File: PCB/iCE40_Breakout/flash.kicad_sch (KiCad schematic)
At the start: 43 parts, among them J1 prog_hdr, Q10 L2N7002SLLT1G, Q11 L2N7002SLLT1G, Q12 L2N7002SLLT1G, Q13 L2N7002SLLT1G, Q14 L2N7002SLLT1G, Q15 L2N7002SLLT1G, Q16 L2N7002SLLT1G, Q6 L2N7002SLLT1G, Q7 L2N7002SLLT1G, Q8 L2N7002SLLT1G, Q9 L2N7002SLLT1G, U6 W25Q128JVS

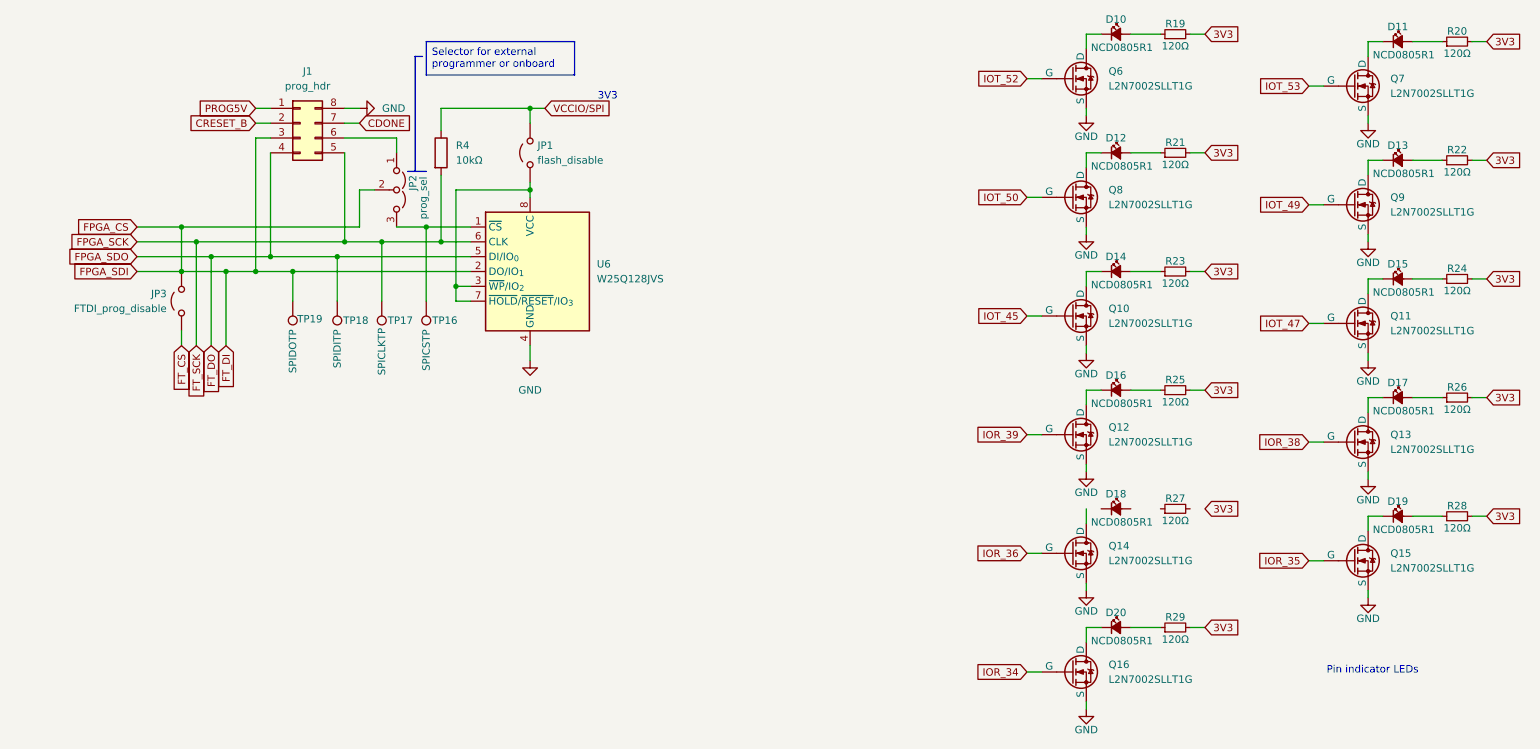
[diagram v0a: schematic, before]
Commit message: Added sheet information, and fixed ERC errors
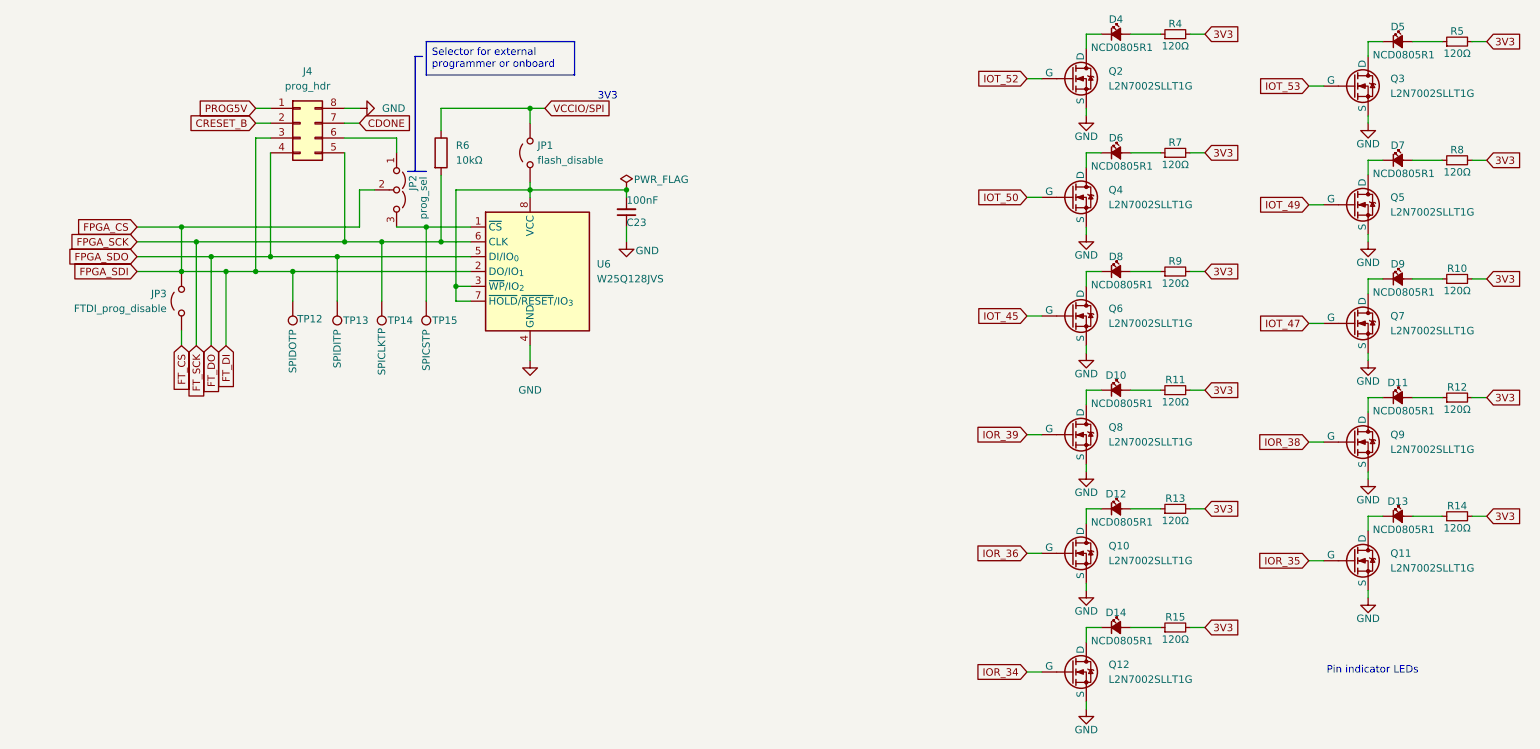
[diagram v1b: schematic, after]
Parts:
- added C23: 100nF, Capacitor_SMD:C_0402_1005Metric, symbol Device:C_Small
- renumbered D16 to D10, D17 to D11, D18 to D12, D19 to D13, D20 to D14, D10 to D4, D11 to D5, D12 to D6, D13 to D7, D14 to D8, D15 to D9, J1 to J4, Q14 to Q10, Q15 to Q11, Q16 to Q12, Q6 to Q2, Q7 to Q3, Q8 to Q4, Q9 to Q5, Q10 to Q6, Q11 to Q7, Q12 to Q8, Q13 to Q9, R24 to R10, R25 to R11, R26 to R12, R27 to R13, R28 to R14, R29 to R15, R19 to R4, R20 to R5, R4 to R6, R21 to R7, R22 to R8, R23 to R9, TP19 to TP12, TP18 to TP13, TP17 to TP14, TP16 to TP15
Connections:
- net 3V3: now also R13.2
- net GND: now also C23.1
- net at R13.1: now also D12.2 (A)
- net at JP1.1 (A), U6.3 (~{WP}/IO_{2}), U6.7 (~{HOLD}/~{RESET}/IO_{3})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: now also C23.2
- net at D12.1 (K): now also Q10.1 (D)
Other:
- company: (none) -> S3I
- title: (none) -> iCE40 Breakout

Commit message: Added missing footprints
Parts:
- J4: footprint (none) -> Connector_PinHeader_2.54mm:PinHeader_2x04_P2.54mm_Vertical
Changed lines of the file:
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@@
 			)
 		)
-		(property "Footprint" ""
+		(property "Footprint" "Connector_PinHeader_2.54mm:PinHeader_2x04_P2.54mm_Vertical"
 			(at 69.85 34.29 0)
 			(effects

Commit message: Changed LED footprints to be from LED lib, and not the Diode lib
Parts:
- D10, D11, D12, D13, D14, D4, D5, D6, D7, D8, D9: footprint Diode_SMD:D_0805_2012Metric -> LED_SMD:LED_0805_2012Metric
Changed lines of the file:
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@@
 			)
 		)
-		(property "Footprint" "Diode_SMD:D_0805_2012Metric"
+		(property "Footprint" "LED_SMD:LED_0805_2012Metric"
 			(at 209.55 120.65 90)
 			(effects
@@
 			)
 		)
-		(property "Footprint" "Diode_SMD:D_0805_2012Metric"
+		(property "Footprint" "LED_SMD:LED_0805_2012Metric"
 			(at 209.55 19.05 90)
 			(effects
@@
 			)
 		)
-		(property "Footprint" "Diode_SMD:D_0805_2012Metric"
+		(property "Footprint" "LED_SMD:LED_0805_2012Metric"
 			(at 209.55 39.37 90)
 			(effects
@@
 			)
 		)
-		(property "Footprint" "Diode_SMD:D_0805_2012Metric"
+		(property "Footprint" "LED_SMD:LED_0805_2012Metric"
 			(at 257.81 81.28 90)
 			(effects
@@
 			)
 		)
-		(property "Footprint" "Diode_SMD:D_0805_2012Metric"
+		(property "Footprint" "LED_SMD:LED_0805_2012Metric"
 			(at 257.81 60.96 90)
 			(effects
@@
 			)
 		)
-		(property "Footprint" "Diode_SMD:D_0805_2012Metric"
+		(property "Footprint" "LED_SMD:LED_0805_2012Metric"
 			(at 209.55 59.69 90)
 			(effects
@@
 			)
 		)
-		(property "Footprint" "Diode_SMD:D_0805_2012Metric"
+		(property "Footprint" "LED_SMD:LED_0805_2012Metric"
 			(at 257.81 101.6 90)
 			(effects
@@
 			)
 		)
-		(property "Footprint" "Diode_SMD:D_0805_2012Metric"
+		(property "Footprint" "LED_SMD:LED_0805_2012Metric"
 			(at 209.55 100.33 90)
 			(effects
@@
 			)
 		)
-		(property "Footprint" "Diode_SMD:D_0805_2012Metric"
+		(property "Footprint" "LED_SMD:LED_0805_2012Metric"
 			(at 209.55 80.01 90)
 			(effects
@@
 			)
 		)
-		(property "Footprint" "Diode_SMD:D_0805_2012Metric"
+		(property "Footprint" "LED_SMD:LED_0805_2012Metric"
 			(at 257.81 40.64 90)
 			(effects
@@
 			)
 		)
-		(property "Footprint" "Diode_SMD:D_0805_2012Metric"
+		(property "Footprint" "LED_SMD:LED_0805_2012Metric"
 			(at 257.81 20.32 90)
 			(effects

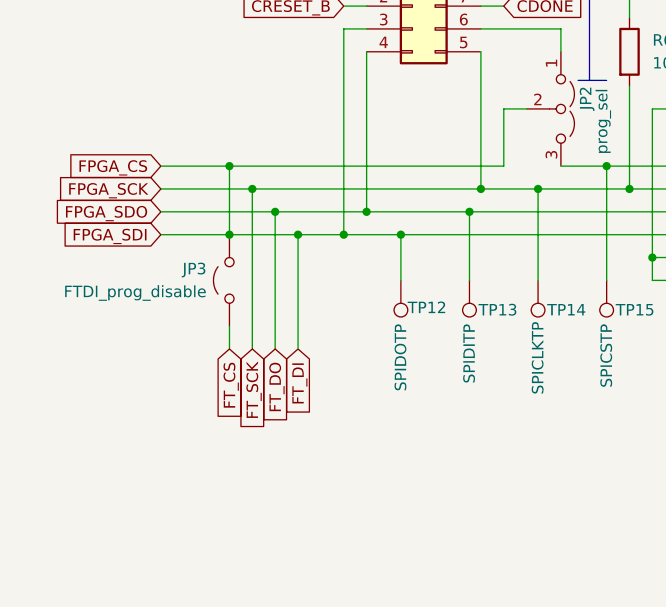
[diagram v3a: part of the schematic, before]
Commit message: Cleaned up SPI flash lines, and removed error where CS was shorted to DI
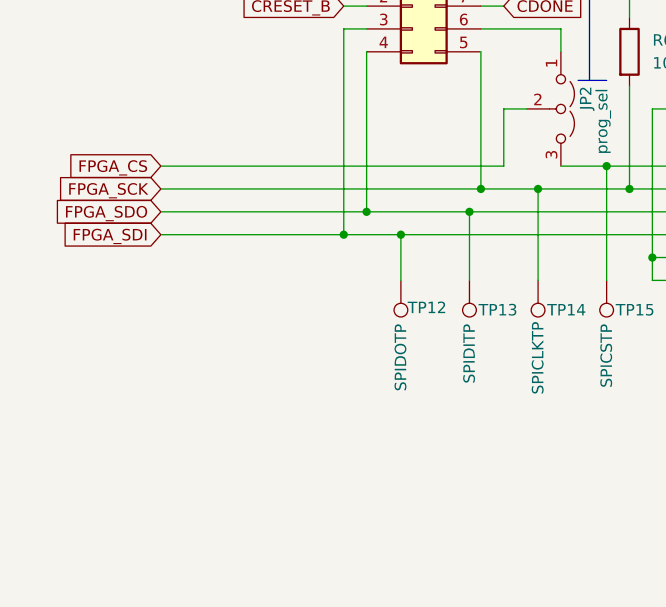
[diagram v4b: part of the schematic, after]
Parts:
- removed JP3: FTDI_prog_disable, Connector_PinSocket_2.54mm:PinSocket_1x02_P2.54mm_Vertical, symbol Jumper:Jumper_2_Open
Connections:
- net FPGA_CS: no longer J4.3 (Pin_3), TP12.1, U6.2 (DO/IO_{1})
- new net FPGA_SDI: J4.3 (Pin_3), TP12.1, U6.2 (DO/IO_{1})

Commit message: Changed jumper footprint to come from jumper library, not generic connector
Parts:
- added R30: 10kΩ, Resistor_SMD:R_0603_1608Metric, symbol Device:R_Small
- JP1: footprint Connector_PinSocket_2.54mm:PinSocket_1x02_P2.54mm_Vertical -> TestPoint:TestPoint_2Pads_Pitch2.54mm_Drill0.8mm
- R6: symbol Device:R -> Device:R_Small
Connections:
- net at C23.2, JP1.1 (A), U6.8 (VCC): now also R30.2; no longer U6.3 (~{WP}/IO_{2}), U6.7 (~{HOLD}/~{RESET}/IO_{3})
- new net: R30.1, U6.3 (~{WP}/IO_{2}), U6.7 (~{HOLD}/~{RESET}/IO_{3})
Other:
- moved on the sheet: R6
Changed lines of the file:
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@@
 	(wire
 		(pts
-			(xy 93.98 43.18) (xy 93.98 54.61)
+			(xy 93.98 39.37) (xy 93.98 54.61)
 		)
 		(stroke
@@
 	(wire
 		(pts
+			(xy 105.41 45.72) (xy 109.22 45.72)
+		)
+		(stroke
+			(width 0)
+			(type default)
+		)
+	)
+	(wire
+		(pts
 			(xy 96.52 62.23) (xy 96.52 64.77)
 		)
@@
 	(wire
 		(pts
-			(xy 96.52 45.72) (xy 109.22 45.72)
+			(xy 96.52 45.72) (xy 100.33 45.72)
 		)
 		(stroke
@@
 	(wire
 		(pts
-			(xy 93.98 31.75) (xy 93.98 35.56)
+			(xy 93.98 31.75) (xy 93.98 34.29)
 		)
 		(stroke
@@
 	)
 	(symbol
-		(lib_id "Device:R")
-		(at 93.98 39.37 0)
+		(lib_id "Device:R_Small")
+		(at 93.98 36.83 0)
 		(unit 1)
 		(exclude_from_sim no)
@@
 		(fields_autoplaced yes)
 		(property "Reference" "R6"
-			(at 96.52 38.0999 0)
+			(at 96.52 35.5599 0)
 			(effects
 				(font
@@
 		)
 		(property "Value" "10kΩ"
-			(at 96.52 40.6399 0)
+			(at 96.52 38.0999 0)
 			(effects
 				(font
@@
 		)
 		(property "Footprint" "Resistor_SMD:R_0603_1608Metric"
-			(at 92.202 39.37 90)
+			(at 93.98 36.83 0)
 			(effects
 				(font
@@
 		)
 		(property "Datasheet" "~"
-			(at 93.98 39.37 0)
+			(at 93.98 36.83 0)
 			(effects
 				(font
@@
 			)
 		)
-		(property "Description" "Resistor"
-			(at 93.98 39.37 0)
+		(property "Description" "Resistor, small symbol"
+			(at 93.98 36.83 0)
 			(effects
 				(font
@@
 		)
 		(property "LCSC" "C25804"
-			(at 93.98 39.37 0)
+			(at 93.98 36.83 0)
 			(effects
 				(font
@@
 	(symbol
 		(lib_id "Device:R_Small")
+		(at 102.87 45.72 90)
+		(unit 1)
+		(exclude_from_sim no)
+		(in_bom yes)
+		(on_board yes)
+		(dnp no)
+		(property "Reference" "R30"
+			(at 102.87 43.942 90)
+			(effects
+				(font
+					(size 1.27 1.27)
+				)
+			)
+		)
+		(property "Value" "10kΩ"
+			(at 102.87 47.498 90)
+			(effects
+				(font
+					(size 1.27 1.27)
+				)
+			)
+		)
+		(property "Footprint" "Resistor_SMD:R_0603_1608Metric"
+			(at 102.87 45.72 0)
+			(effects
+				(font
+					(size 1.27 1.27)
+				)
+				(hide yes)
+			)
+		)
+		(property "Datasheet" "~"
+			(at 102.87 45.72 0)
+			(effects
+				(font
+					(size 1.27 1.27)
+				)
+				(hide yes)
+			)
+		)
+		(property "Description" "Resistor, small symbol"
+			(at 102.87 45.72 0)
+			(effects
+				(font
+					(size 1.27 1.27)
+				)
+				(hide yes)
+			)
+		)
+		(property "LCSC" "C25804"
+			(at 102.87 45.72 0)
+			(effects
+				(font
+					(size 1.27 1.27)
+				)
+				(hide yes)
+			)
+		)
+		(pin "1"
+		)
+		(pin "2"
+		)
+		(instances
+			(project "iCE40_Breakout"
+				(path "/ce4d7974-ef38-4eea-8119-381c4298ef02/0b13b405-f1f0-4313-93f2-3939760c2f72"
+					(reference "R30")
+					(unit 1)
+				)
+			)
+		)
+	)
+	(symbol
+		(lib_id "Device:R_Small")
 		(at 267.97 101.6 90)
 		(unit 1)
@@
 			)
 		)
-		(property "Footprint" "Connector_PinSocket_2.54mm:PinSocket_1x02_P2.54mm_Vertical"
+		(property "Footprint" "TestPoint:TestPoint_2Pads_Pitch2.54mm_Drill0.8mm"
 			(at 109.22 39.37 0)
 			(effects

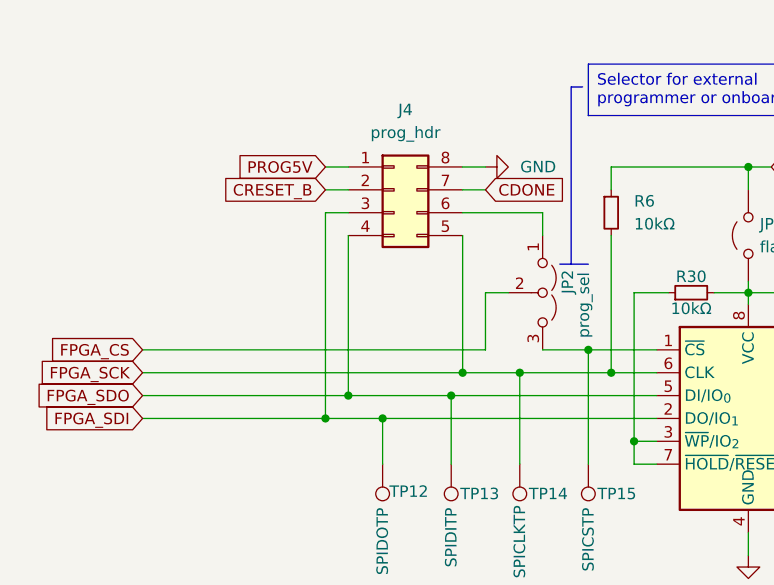
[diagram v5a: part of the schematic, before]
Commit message: Changed JP2 wiring so that CS can be switched between FTDI chip and external programming header
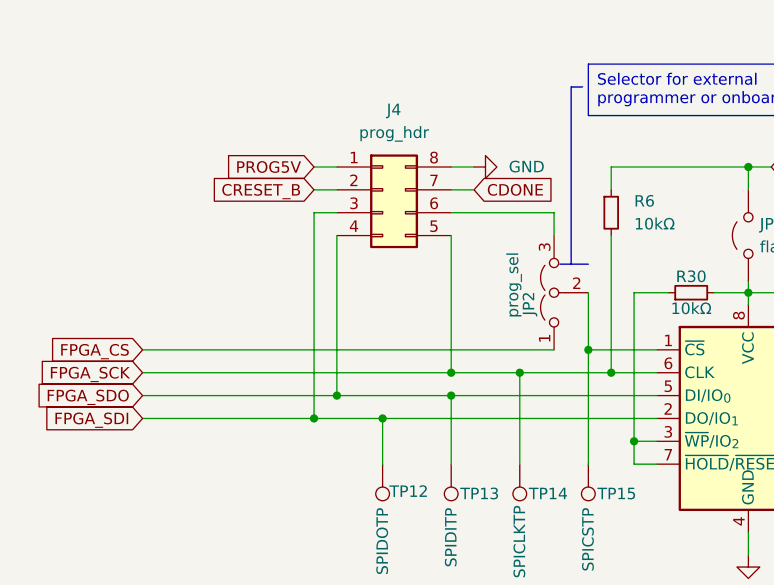
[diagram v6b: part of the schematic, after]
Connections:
- net FPGA_CS: now also JP2.1 (A); no longer JP2.2 (C)
- net at J4.6 (Pin_6): now also JP2.3 (B); no longer JP2.1 (A)
- net at TP15.1, U6.1 (~{CS}): now also JP2.2 (C); no longer JP2.3 (B)
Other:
- moved on the sheet: J4, JP2
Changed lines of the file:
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@@
 	)
 	(junction
-		(at 109.22 31.75)
+		(at 63.5 57.15)
 		(diameter 0)
 		(color 0 0 0 0)
 	)
 	(junction
-		(at 96.52 62.23)
+		(at 60.96 59.69)
 		(diameter 0)
 		(color 0 0 0 0)
 	)
 	(junction
-		(at 62.23 59.69)
+		(at 109.22 31.75)
 		(diameter 0)
 		(color 0 0 0 0)
 	)
 	(junction
-		(at 93.98 54.61)
+		(at 96.52 62.23)
 		(diameter 0)
 		(color 0 0 0 0)
 	)
 	(junction
-		(at 76.2 57.15)
+		(at 76.2 54.61)
 		(diameter 0)
 		(color 0 0 0 0)
 	)
 	(junction
-		(at 68.58 59.69)
+		(at 93.98 54.61)
 		(diameter 0)
 		(color 0 0 0 0)
 	)
 	(junction
-		(at 83.82 54.61)
+		(at 76.2 57.15)
 		(diameter 0)
 		(color 0 0 0 0)
 	)
 	(junction
-		(at 64.77 57.15)
+		(at 68.58 59.69)
 		(diameter 0)
 		(color 0 0 0 0)
 	)
 	(junction
-		(at 109.22 45.72)
+		(at 83.82 54.61)
 		(diameter 0)
 		(color 0 0 0 0)
 	)
 	(junction
-		(at 91.44 52.07)
+		(at 109.22 45.72)
 		(diameter 0)
 		(color 0 0 0 0)
 	)
 	(junction
-		(at 77.47 54.61)
+		(at 91.44 52.07)
 		(diameter 0)
 		(color 0 0 0 0)
@@
 	(wire
 		(pts
-			(xy 62.23 31.75) (xy 64.77 31.75)
+			(xy 60.96 31.75) (xy 63.5 31.75)
 		)
 		(stroke
@@
 	(wire
 		(pts
-			(xy 41.91 52.07) (xy 80.01 52.07)
+			(xy 41.91 52.07) (xy 87.63 52.07)
 		)
 		(stroke
@@
 	(wire
 		(pts
+			(xy 91.44 45.72) (xy 91.44 52.07)
+		)
+		(stroke
+			(width 0)
+			(type default)
+		)
+	)
+	(wire
+		(pts
 			(xy 212.09 19.05) (xy 217.17 19.05)
 		)
@@
 	(wire
 		(pts
-			(xy 62.23 34.29) (xy 64.77 34.29)
+			(xy 60.96 34.29) (xy 63.5 34.29)
 		)
 		(stroke
@@
 	(wire
 		(pts
-			(xy 77.47 34.29) (xy 80.01 34.29)
+			(xy 76.2 34.29) (xy 78.74 34.29)
 		)
 		(stroke
@@
 	(wire
 		(pts
-			(xy 62.23 59.69) (xy 68.58 59.69)
+			(xy 63.5 57.15) (xy 76.2 57.15)
 		)
 		(stroke
@@
 	(wire
 		(pts
-			(xy 64.77 36.83) (xy 62.23 36.83)
+			(xy 63.5 36.83) (xy 60.96 36.83)
 		)
 		(stroke
@@
 	(wire
 		(pts
-			(xy 77.47 36.83) (xy 86.36 36.83)
+			(xy 76.2 36.83) (xy 87.63 36.83)
 		)
 		(stroke
@@
 	(wire
 		(pts
-			(xy 77.47 31.75) (xy 80.01 31.75)
+			(xy 76.2 31.75) (xy 78.74 31.75)
 		)
 		(stroke
@@
 	(wire
 		(pts
-			(xy 64.77 39.37) (xy 64.77 57.15)
+			(xy 63.5 39.37) (xy 63.5 57.15)
 		)
 		(stroke
@@
 	(wire
 		(pts
-			(xy 41.91 54.61) (xy 77.47 54.61)
+			(xy 41.91 54.61) (xy 76.2 54.61)
 		)
 		(stroke
@@
 	(wire
 		(pts
+			(xy 76.2 54.61) (xy 83.82 54.61)
+		)
+		(stroke
+			(width 0)
+			(type default)
+		)
+	)
+	(wire
+		(pts
 			(xy 252.73 114.3) (xy 252.73 115.57)
 		)
@@
 	(wire
 		(pts
-			(xy 86.36 36.83) (xy 86.36 39.37)
+			(xy 87.63 36.83) (xy 87.63 39.37)
 		)
 		(stroke
@@
 	(wire
 		(pts
-			(xy 64.77 57.15) (xy 76.2 57.15)
-		)
-		(stroke
-			(width 0)
-			(type default)
-		)
-	)
-	(wire
-		(pts
 			(xy 222.25 19.05) (xy 224.79 19.05)
 		)
@@
 	(wire
 		(pts
-			(xy 41.91 57.15) (xy 64.77 57.15)
-		)
-		(stroke
-			(width 0)
-			(type default)
-		)
-	)
-	(wire
-		(pts
-			(xy 77.47 39.37) (xy 77.47 54.61)
+			(xy 41.91 57.15) (xy 63.5 57.15)
 		)
 		(stroke
@@
 	(wire
 		(pts
-			(xy 77.47 54.61) (xy 83.82 54.61)
+			(xy 76.2 39.37) (xy 76.2 54.61)
 		)
 		(stroke
@@
 	(wire
 		(pts
-			(xy 41.91 59.69) (xy 62.23 59.69)
+			(xy 41.91 59.69) (xy 60.96 59.69)
 		)
 		(stroke
@@
 	(wire
 		(pts
-			(xy 80.01 52.07) (xy 80.01 45.72)
+			(xy 60.96 59.69) (xy 68.58 59.69)
 		)
 		(stroke
@@
 	(wire
 		(pts
-			(xy 80.01 45.72) (xy 82.55 45.72)
-		)
-		(stroke
-			(width 0)
-			(type default)
-		)
-	)
-	(wire
-		(pts
 			(xy 252.73 104.14) (xy 252.73 101.6)
 		)
@@
 	(wire
 		(pts
-			(xy 86.36 52.07) (xy 91.44 52.07)
-		)
-		(stroke
-			(width 0)
-			(type default)
-		)
-	)
-	(wire
-		(pts
 			(xy 109.22 34.29) (xy 109.22 31.75)
 		)
@@
 	(wire
 		(pts
-			(xy 62.23 36.83) (xy 62.23 59.69)
+			(xy 60.96 36.83) (xy 60.96 59.69)
 		)
 		(stroke
@@
 	(global_label "PROG5V"
 		(shape input)
-		(at 62.23 31.75 180)
+		(at 60.96 31.75 180)
 		(fields_autoplaced yes)
 		(effects
@@
 		)
 		(property "Intersheetrefs" "${INTERSHEET_REFS}"
-			(at 51.8062 31.75 0)
+			(at 50.5362 31.75 0)
 			(effects
 				(font
@@
 	(global_label "CRESET_B"
 		(shape input)
-		(at 62.23 34.29 180)
+		(at 60.96 34.29 180)
 		(fields_autoplaced yes)
 		(effects
@@
 		)
 		(property "Intersheetrefs" "${INTERSHEET_REFS}"
-			(at 49.9921 34.29 0)
+			(at 48.7221 34.29 0)
 			(effects
 				(font
@@
 	(global_label "CDONE"
 		(shape input)
-		(at 80.01 34.29 0)
+		(at 78.74 34.29 0)
 		(fields_autoplaced yes)
 		(effects
@@
 		)
 		(property "Intersheetrefs" "${INTERSHEET_REFS}"
-			(at 89.3452 34.29 0)
+			(at 88.0752 34.29 0)
 			(effects
 				(font
@@
 	(symbol
 		(lib_id "Connector_Generic:Conn_02x04_Counter_Clockwise")
-		(at 69.85 34.29 0)
+		(at 68.58 34.29 0)
 		(unit 1)
 		(exclude_from_sim no)
@@
 		(fields_autoplaced yes)
 		(property "Reference" "J4"
-			(at 71.12 25.4 0)
+			(at 69.85 25.4 0)
 			(effects
 				(font
@@
 		)
 		(property "Value" "prog_hdr"
-			(at 71.12 27.94 0)
+			(at 69.85 27.94 0)
 			(effects
 				(font
@@
 		)
 		(property "Footprint" "Connector_PinHeader_2.54mm:PinHeader_2x04_P2.54mm_Vertical"
-			(at 69.85 34.29 0)
+			(at 68.58 34.29 0)
 			(effects
 				(font
@@
 		)
 		(property "Datasheet" "~"
-			(at 69.85 34.29 0)
+			(at 68.58 34.29 0)
 			(effects
 				(font
@@
 		)
 		(property "Description" "Generic connector, double row, 02x04, counter clockwise pin numbering scheme (similar to DIP package numbering), script generated (kicad-library-utils/schlib/autogen/connector/)"
-			(at 69.85 34.29 0)
+			(at 68.58 34.29 0)
 			(effects
 				(font
@@
 	(symbol
 		(lib_id "Jumper:Jumper_3_Open")
-		(at 86.36 45.72 270)
+		(at 87.63 45.72 90)
 		(unit 1)
 		(exclude_from_sim no)
@@
 		(dnp no)
 		(property "Reference" "JP2"
-			(at 89.154 43.18 0)
+			(at 84.836 48.26 0)
 			(effects
 				(font
@@
 		)
 		(property "Value" "prog_sel"
-			(at 90.932 43.434 0)
+			(at 83.058 48.514 0)
 			(effects
 				(font
@@
 		)
 		(property "Footprint" "Connector_PinSocket_2.54mm:PinSocket_1x03_P2.54mm_Vertical"
-			(at 86.36 45.72 0)
+			(at 87.63 45.72 0)
 			(effects
 				(font
@@
 		)
 		(property "Datasheet" "~"
-			(at 86.36 45.72 0)
+			(at 87.63 45.72 0)
 			(effects
 				(font
@@
 		)
 		(property "Description" "Jumper, 3-pole, both open"
-			(at 86.36 45.72 0)
+			(at 87.63 45.72 0)
 			(effects
 				(font
@@
 	(symbol
 		(lib_id "power:GND")
-		(at 80.01 31.75 90)
+		(at 78.74 31.75 90)
 		(unit 1)
 		(exclude_from_sim no)
@@
 		(fields_autoplaced yes)
 		(property "Reference" "#PWR026"
-			(at 86.36 31.75 0)
+			(at 85.09 31.75 0)
 			(effects
 				(font
@@
 		)
 		(property "Value" "GND"
-			(at 83.8667 31.7499 90)
+			(at 82.5967 31.7499 90)
 			(effects
 				(font
@@
 		)
 		(property "Footprint" ""
-			(at 80.01 31.75 0)
+			(at 78.74 31.75 0)
 			(effects
 				(font
@@
 		)
 		(property "Datasheet" ""
-			(at 80.01 31.75 0)
+			(at 78.74 31.75 0)
 			(effects
 				(font
@@
 		)
 		(property "Description" "Power symbol creates a global label with name \"GND\" , ground"
-			(at 80.01 31.75 0)
+			(at 78.74 31.75 0)
 			(effects
 				(font
